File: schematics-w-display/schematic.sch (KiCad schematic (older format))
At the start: 4 parts, among them J1 Conn_01x21_Female, J2 Conn_01x06_Female, J3 Conn_01x21_Female, J4 Conn_01x08_Female

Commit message: Maybe not so final version
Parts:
- J4: footprint Connector_JST:JST_PH_B8B-PH-K_1x08_P2.00mm_Vertical -> Connector_JST:JST_PH_S8B-PH-K_1x08_P2.00mm_Horizontal
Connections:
- net 3v3: now also J4.1 (Pin_1); no longer J4.8 (Pin_8)
- net BUSY: now also J4.8 (Pin_8); no longer J4.1 (Pin_1)
- net CLK: now also J4.4 (Pin_4); no longer J4.5 (Pin_5)
- net CS: now also J4.5 (Pin_5); no longer J4.4 (Pin_4)
- net DC: now also J4.6 (Pin_6); no longer J4.3 (Pin_3)
- net GND: now also J4.2 (Pin_2); no longer J4.7 (Pin_7)
- net MOSI: now also J4.3 (Pin_3); no longer J4.6 (Pin_6)
- net RST: now also J4.7 (Pin_7); no longer J4.2 (Pin_2)
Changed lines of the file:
@@
 L Connector:Conn_01x08_Female J4
 U 1 1 60EB76B2
-P 3050 4050
-F 0 "J4" H 2942 3425 50  0000 C CNN
-F 1 "Conn_01x08_Female" H 2942 3516 50  0000 C CNN
-F 2 "Connector_JST:JST_PH_B8B-PH-K_1x08_P2.00mm_Vertical" H 3050 4050 50  0001 C CNN
-F 3 "~" H 3050 4050 50  0001 C CNN
-	1    3050 4050
-	-1   0    0    1
+P 3250 3950
+F 0 "J4" H 3142 3325 50  0000 C CNN
+F 1 "Conn_01x08_Female" H 3142 3416 50  0000 C CNN
+F 2 "Connector_JST:JST_PH_S8B-PH-K_1x08_P2.00mm_Horizontal" H 3250 3950 50  0001 C CNN
+F 3 "~" H 3250 3950 50  0001 C CNN
+	1    3250 3950
+	1    0    0    -1
 $EndComp
 Text GLabel 3550 3750 2    50   Input ~ 0
@@
 	3900 3100 3900 3650
 Wire Wire Line
-	3900 3650 3250 3650
-Wire Wire Line
-	3250 4350 3500 4350
-Wire Wire Line
 	3500 4350 3500 4800
 Wire Wire Line
 	3500 4800 4400 4800
-Wire Wire Line
-	3250 4250 3600 4250
 Wire Wire Line
 	3600 4250 3600 4700
@@
 	3600 4700 4400 4700
 Wire Wire Line
-	3250 4150 3700 4150
-Wire Wire Line
 	3700 4150 3700 4600
 Wire Wire Line
 	3700 4600 4400 4600
-Wire Wire Line
-	3250 4050 3800 4050
 Wire Wire Line
 	3800 4050 3800 4500
@@
 	3800 4500 4400 4500
 Wire Wire Line
-	3250 3950 3900 3950
-Wire Wire Line
 	3900 3950 3900 4400
 Wire Wire Line
 	3900 4400 4400 4400
-Wire Wire Line
-	3250 3850 4000 3850
 Wire Wire Line
 	4000 3850 4000 4300
@@
 Text Label 3250 3850 0    50   ~ 0
 MOSI
-Wire Wire Line
-	3250 3750 3550 3750
 Text Label 3250 3950 0    50   ~ 0
 CLK
@@
 	3900 3100 4400 3100
 Connection ~ 4400 3100
+Wire Wire Line
+	3050 3650 3900 3650
+Wire Wire Line
+	3050 3750 3550 3750
+Wire Wire Line
+	3050 3850 4000 3850
+Wire Wire Line
+	3050 3950 3900 3950
+Wire Wire Line
+	3050 4050 3800 4050
+Wire Wire Line
+	3050 4150 3700 4150
+Wire Wire Line
+	3050 4250 3600 4250
+Wire Wire Line
+	3050 4350 3500 4350
 $EndSCHEMATC

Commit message: Some schematic prettify
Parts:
- added SW1: Bootloader_Push, Button_Switch_THT:SW_PUSH_6mm, symbol Switch:SW_Push
- added SW2: RST_Push, Button_Switch_THT:SW_Tactile_SKHH_Angled, symbol Switch:SW_Push
- J1, J3: value Conn_01x21_Female -> Conn_01x21_Female_ESP
- J2: value Conn_01x06_Female -> Conn_01x06_Female_BME280
- J4: value Conn_01x08_Female -> Conn_01x08_Female_Display
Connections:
- net GND: now also SW1.1, SW2.2
- net at J1.2 (Pin_2): now also SW2.1
- net at J3.20 (Pin_20): now also SW1.2
- no-connect marks 29 -> 27
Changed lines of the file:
@@
 P 5450 4100
 F 0 "J1" H 5478 4126 50  0000 L CNN
-F 1 "Conn_01x21_Female" H 5478 4035 50  0000 L CNN
+F 1 "Conn_01x21_Female_ESP" H 5478 4035 50  0000 L CNN
 F 2 "Connector_PinHeader_2.54mm:PinHeader_1x21_P2.54mm_Vertical" H 5450 4100 50  0001 C CNN
 F 3 "~" H 5450 4100 50  0001 C CNN
@@
 P 4750 2400
 F 0 "J2" V 4688 2012 50  0000 R CNN
-F 1 "Conn_01x06_Female" V 4597 2012 50  0000 R CNN
+F 1 "Conn_01x06_Female_BME280" V 4597 2012 50  0000 R CNN
 F 2 "Connector_PinHeader_2.54mm:PinHeader_1x06_P2.54mm_Vertical" H 4750 2400 50  0001 C CNN
 F 3 "~" H 4750 2400 50  0001 C CNN
@@
 NoConn ~ 5250 3400
 NoConn ~ 5250 3300
-NoConn ~ 5250 3200
 NoConn ~ 4400 3800
 NoConn ~ 4400 3700
 NoConn ~ 4400 5000
 NoConn ~ 4400 4900
-NoConn ~ 4400 3200
 NoConn ~ 4400 4200
 NoConn ~ 4400 4100
@@
 P 4200 4100
 F 0 "J3" H 4092 2875 50  0000 C CNN
-F 1 "Conn_01x21_Female" H 4092 2966 50  0000 C CNN
+F 1 "Conn_01x21_Female_ESP" H 4092 2966 50  0000 C CNN
 F 2 "Connector_PinHeader_2.54mm:PinHeader_1x21_P2.54mm_Vertical" H 4200 4100 50  0001 C CNN
 F 3 "~" H 4200 4100 50  0001 C CNN
@@
 P 3250 3950
 F 0 "J4" H 3142 3325 50  0000 C CNN
-F 1 "Conn_01x08_Female" H 3142 3416 50  0000 C CNN
+F 1 "Conn_01x08_Female_Display" H 3142 3416 50  0000 C CNN
 F 2 "Connector_JST:JST_PH_S8B-PH-K_1x08_P2.00mm_Horizontal" H 3250 3950 50  0001 C CNN
 F 3 "~" H 3250 3950 50  0001 C CNN
@@
 Wire Wire Line
 	3050 4350 3500 4350
+$Comp
+L Switch:SW_Push SW1
+U 1 1 610E97B1
+P 3450 3200
+F 0 "SW1" H 3450 3485 50  0000 C CNN
+F 1 "Bootloader_Push" H 3450 3394 50  0000 C CNN
+F 2 "Button_Switch_THT:SW_PUSH_6mm" H 3450 3400 50  0001 C CNN
+F 3 "~" H 3450 3400 50  0001 C CNN
+	1    3450 3200
+	1    0    0    -1
+$EndComp
+Wire Wire Line
+	3650 3200 4400 3200
+Text GLabel 3250 3200 0    50   Input ~ 0
+GND
+$Comp
+L Switch:SW_Push SW2
+U 1 1 610ECECB
+P 5900 3200
+F 0 "SW2" H 5900 3485 50  0000 C CNN
+F 1 "RST_Push" H 5900 3394 50  0000 C CNN
+F 2 "Button_Switch_THT:SW_Tactile_SKHH_Angled" H 5900 3400 50  0001 C CNN
+F 3 "~" H 5900 3400 50  0001 C CNN
+	1    5900 3200
+	1    0    0    -1
+$EndComp
+Wire Wire Line
+	5250 3200 5700 3200
+Text GLabel 6100 3200 2    50   Input ~ 0
+GND
 $EndSCHEMATC

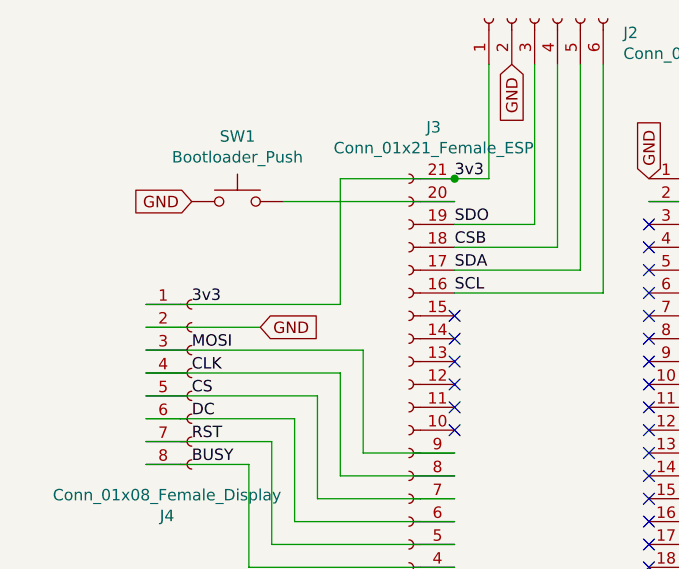
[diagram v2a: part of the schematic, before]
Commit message: Add LDR to schematic
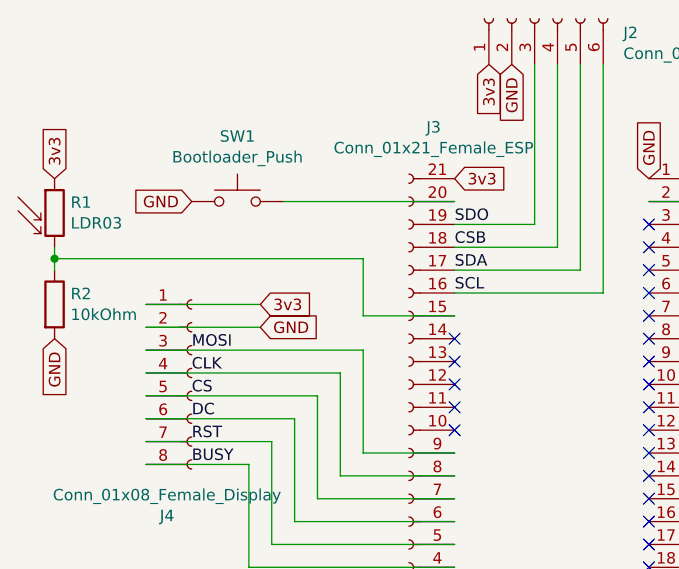
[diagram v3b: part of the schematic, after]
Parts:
- added R1: LDR03, Connector_PinHeader_2.54mm:PinHeader_1x02_P2.54mm_Vertical, symbol Sensor_Optical:LDR03
- added R2: 10kOhm, Connector_PinHeader_2.54mm:PinHeader_1x02_P2.54mm_Vertical, symbol Device:R
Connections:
- net 3v3: now also R1.1
- net GND: now also R2.2
- net at J3.15 (Pin_15): now also R1.2, R2.1
- no-connect marks 27 -> 26
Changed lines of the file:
@@
 	0    -1   -1   0
 $EndComp
-Text Label 4400 3100 0    50   ~ 0
-3v3
 Text Label 4400 3300 0    50   ~ 0
 SDO
@@
 NoConn ~ 5250 3300
 NoConn ~ 4400 3800
-NoConn ~ 4400 3700
 NoConn ~ 4400 5000
 NoConn ~ 4400 4900
@@
 SCL
 Wire Wire Line
-	4400 3100 4550 3100
-Wire Wire Line
-	4550 3100 4550 2600
-Wire Wire Line
 	4400 3300 4750 3300
 Wire Wire Line
@@
 Text GLabel 3550 3750 2    50   Input ~ 0
 GND
-Wire Wire Line
-	3900 3100 3900 3650
 Wire Wire Line
 	3500 4350 3500 4800
@@
 Text Label 3250 4350 0    50   ~ 0
 BUSY
-Text Label 3250 3650 0    50   ~ 0
-3v3
-Wire Wire Line
-	3900 3100 4400 3100
-Connection ~ 4400 3100
-Wire Wire Line
-	3050 3650 3900 3650
 Wire Wire Line
 	3050 3750 3550 3750
@@
 Text GLabel 6100 3200 2    50   Input ~ 0
 GND
+$Comp
+L Sensor_Optical:LDR03 R1
+U 1 1 613275E0
+P 2650 3250
+F 0 "R1" H 2720 3296 50  0000 L CNN
+F 1 "LDR03" H 2720 3205 50  0000 L CNN
+F 2 "Connector_PinHeader_2.54mm:PinHeader_1x02_P2.54mm_Vertical" V 2825 3250 50  0001 C CNN
+F 3 "http://www.elektronica-componenten.nl/WebRoot/StoreNL/Shops/61422969/54F1/BA0C/C664/31B9/2173/C0A8/2AB9/2AEF/LDR03IMP.pdf" H 2650 3200 50  0001 C CNN
+	1    2650 3250
+	1    0    0    -1
+$EndComp
+$Comp
+L Device:R R2
+U 1 1 613286A5
+P 2650 3650
+F 0 "R2" H 2720 3696 50  0000 L CNN
+F 1 "10kOhm" H 2720 3605 50  0000 L CNN
+F 2 "Connector_PinHeader_2.54mm:PinHeader_1x02_P2.54mm_Vertical" V 2580 3650 50  0001 C CNN
+F 3 "~" H 2650 3650 50  0001 C CNN
+	1    2650 3650
+	1    0    0    -1
+$EndComp
+Text GLabel 2650 3800 3    50   Input ~ 0
+GND
+Text GLabel 2650 3100 1    50   Input ~ 0
+3v3
+Wire Wire Line
+	4400 3700 4000 3700
+Wire Wire Line
+	4000 3700 4000 3450
+Wire Wire Line
+	2650 3450 2650 3400
+Wire Wire Line
+	2650 3450 4000 3450
+Wire Wire Line
+	2650 3500 2650 3450
+Connection ~ 2650 3450
+Text GLabel 3550 3650 2    50   Input ~ 0
+3v3
+Wire Wire Line
+	3050 3650 3550 3650
+Text GLabel 4550 2600 3    50   Input ~ 0
+3v3
+Text GLabel 4400 3100 2    50   Input ~ 0
+3v3
 $EndSCHEMATC

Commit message: Remove LDR, add serial converter
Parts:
- removed R1: LDR03, Connector_PinHeader_2.54mm:PinHeader_1x02_P2.54mm_Vertical, symbol Sensor_Optical:LDR03
- removed R2: 10kOhm, Connector_PinHeader_2.54mm:PinHeader_1x02_P2.54mm_Vertical, symbol Device:R
- added J5: Conn_01x06_Female_RS232_USB, Connector_PinHeader_2.54mm:PinHeader_1x06_P2.54mm_Vertical, symbol Connector:Conn_01x06_Female
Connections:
- net 3v3: now also J5.1 (Pin_1)
- net GND: now also J5.5 (Pin_5)
- net RX-TX: now reaches J1.5 (Pin_5)
- net RX-TX: now also J5.4 (Pin_4)
- net TX-RX: now reaches J1.6 (Pin_6)
- net TX-RX: now also J5.3 (Pin_3)
- no-connect marks 26 -> 27
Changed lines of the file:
@@
 U 1 1 604CADD6
 P 5450 4100
-F 0 "J1" H 5478 4126 50  0000 L CNN
-F 1 "Conn_01x21_Female_ESP" H 5478 4035 50  0000 L CNN
+F 0 "J1" H 5300 2900 50  0000 L CNN
+F 1 "Conn_01x21_Female_ESP" H 4950 3000 50  0000 L CNN
 F 2 "Connector_PinHeader_2.54mm:PinHeader_1x21_P2.54mm_Vertical" H 5450 4100 50  0001 C CNN
 F 3 "~" H 5450 4100 50  0001 C CNN
@@
 NoConn ~ 5250 3800
 NoConn ~ 5250 3700
-NoConn ~ 5250 3600
-NoConn ~ 5250 3500
 NoConn ~ 5250 3400
 NoConn ~ 5250 3300
@@
 Text GLabel 6100 3200 2    50   Input ~ 0
 GND
-$Comp
-L Sensor_Optical:LDR03 R1
-U 1 1 613275E0
-P 2650 3250
-F 0 "R1" H 2720 3296 50  0000 L CNN
-F 1 "LDR03" H 2720 3205 50  0000 L CNN
-F 2 "Connector_PinHeader_2.54mm:PinHeader_1x02_P2.54mm_Vertical" V 2825 3250 50  0001 C CNN
-F 3 "http://www.elektronica-componenten.nl/WebRoot/StoreNL/Shops/61422969/54F1/BA0C/C664/31B9/2173/C0A8/2AB9/2AEF/LDR03IMP.pdf" H 2650 3200 50  0001 C CNN
-	1    2650 3250
-	1    0    0    -1
-$EndComp
-$Comp
-L Device:R R2
-U 1 1 613286A5
-P 2650 3650
-F 0 "R2" H 2720 3696 50  0000 L CNN
-F 1 "10kOhm" H 2720 3605 50  0000 L CNN
-F 2 "Connector_PinHeader_2.54mm:PinHeader_1x02_P2.54mm_Vertical" V 2580 3650 50  0001 C CNN
-F 3 "~" H 2650 3650 50  0001 C CNN
-	1    2650 3650
-	1    0    0    -1
-$EndComp
-Text GLabel 2650 3800 3    50   Input ~ 0
-GND
-Text GLabel 2650 3100 1    50   Input ~ 0
-3v3
-Wire Wire Line
-	4400 3700 4000 3700
-Wire Wire Line
-	4000 3700 4000 3450
-Wire Wire Line
-	2650 3450 2650 3400
-Wire Wire Line
-	2650 3450 4000 3450
-Wire Wire Line
-	2650 3500 2650 3450
-Connection ~ 2650 3450
 Text GLabel 3550 3650 2    50   Input ~ 0
 3v3
@@
 Text GLabel 4400 3100 2    50   Input ~ 0
 3v3
+Text GLabel 6350 3650 0    50   Input ~ 0
+3v3
+Wire Wire Line
+	5250 3500 5750 3500
+Text Label 5500 3500 0    50   ~ 0
+RX-TX
+Text Label 5500 3600 0    50   ~ 0
+TX-RX
+Wire Wire Line
+	5250 3600 5650 3600
+NoConn ~ 6350 3750
+NoConn ~ 6350 4150
+$Comp
+L Connector:Conn_01x06_Female J5
+U 1 1 62A72A06
+P 6550 3850
+F 0 "J5" H 6578 3826 50  0000 L CNN
+F 1 "Conn_01x06_Female_RS232_USB" H 6578 3735 50  0000 L CNN
+F 2 "Connector_PinHeader_2.54mm:PinHeader_1x06_P2.54mm_Vertical" H 6550 3850 50  0001 C CNN
+F 3 "~" H 6550 3850 50  0001 C CNN
+	1    6550 3850
+	1    0    0    -1
+$EndComp
+Text GLabel 6350 4050 0    50   Input ~ 0
+GND
+Wire Wire Line
+	6350 3950 5750 3950
+Wire Wire Line
+	5750 3500 5750 3950
+Wire Wire Line
+	6350 3850 5650 3850
+Wire Wire Line
+	5650 3850 5650 3600
+NoConn ~ 4400 3700
 $EndSCHEMATC
